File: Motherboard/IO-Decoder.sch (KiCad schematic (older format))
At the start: 7 parts, among them U28 8288, U29 74LS245, U30 74LS04, U31 74LS573, U32 74LS244, U33 74LS573

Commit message: Large sync
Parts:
- added RN2: R_Network04, Resistor_THT:R_Array_SIP5, symbol Device:R_Network04
- added U40: 74LS27, Housings_DIP:DIP-14_W7.62mm_Socket, symbol 74xx:74LS27
- added U41: 74LS04, Housings_DIP:DIP-14_W7.62mm_Socket, symbol 74xx:74LS04
- added U43, U44, U45: 74LS244, Housings_DIP:DIP-20_W7.62mm_Socket, symbol 74xx:74LS244
- added U46: 74LS245, Housings_DIP:DIP-20_W7.62mm_Socket, symbol 74xx:74LS245
- added U47: 4077, Housings_DIP:DIP-14_W7.62mm_Socket, symbol 4xxx:4077
- added U48: SST39SF010, Housings_DIP:DIP-32_W15.24mm_Socket, symbol Memory_Flash:SST39SF010
- added U49: 74LS243, Housings_DIP:DIP-12_W7.62mm_Socket, symbol 74xx:74LS243
- U29, U31, U32, U33: footprint (none) -> Housings_DIP:DIP-20_W7.62mm_Socket
- U30: footprint (none) -> Housings_DIP:DIP-14_W7.62mm_Socket
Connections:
- net labels added: AEN, CLK33, DACK0_BRD, DCLK, ROMADDR, XA0, XA1, XA10, XA11, XA12, XA13, XA14, XA15, XA16, XA17, XA18, XA19, XA2, XA3, XA4, XA5, XA6, XA7, XA8, XA9, XA[0...19], XCLK, XD0, XD1, XD2, XD3, XD4, XD5, XD6, XD7, XD[0...7], ~CS6, ~CS7, ~DACK0, ~DMAAEN, ~IOR, ~MEMR, ~XIOR, ~XIOW, ~XMEMR, ~XMEMW, ~YMEMW
- wire segments 91 -> 230
- no-connect marks 11 -> 13

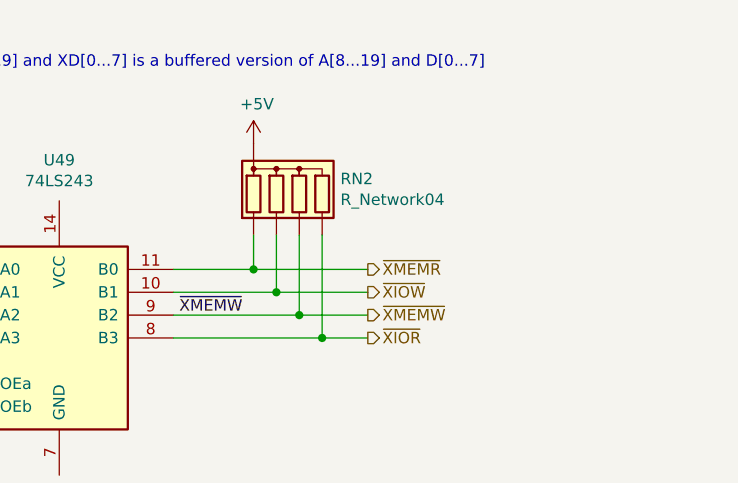
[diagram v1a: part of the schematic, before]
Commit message: Work on motherboard  - Integrating glue logic into CPLD  - Began work on routing
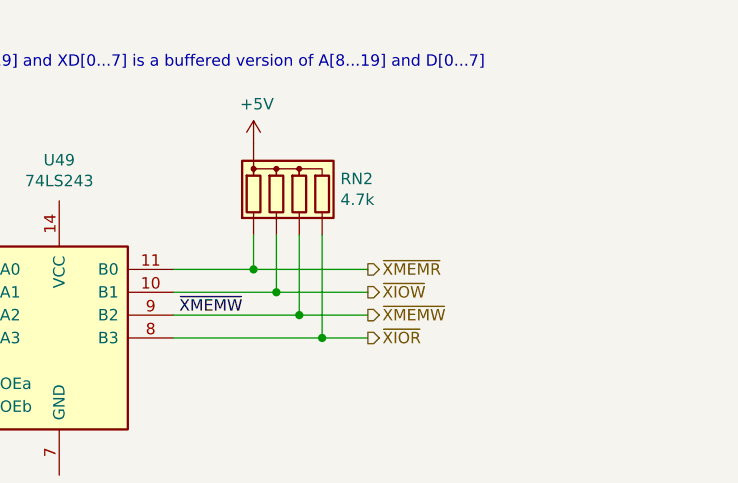
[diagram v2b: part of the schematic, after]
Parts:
- RN1: footprint Resistor_THT:R_Array_SIP6 -> Resistors_THT:R_Array_SIP6
- RN2: value R_Network04 -> 4.7k; footprint Resistor_THT:R_Array_SIP5 -> Resistors_THT:R_Array_SIP5
- U28: footprint Package_DIP:DIP-20_W7.62mm -> Housings_DIP:DIP-20_W7.62mm_Socket
- U49: footprint Housings_DIP:DIP-12_W7.62mm_Socket -> Housings_DIP:DIP-14_W7.62mm_Socket
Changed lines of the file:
@@
 F 0 "U28" H 2300 2800 50  0000 C CNN
 F 1 "8288" H 2300 2725 50  0000 C CNN
-F 2 "Package_DIP:DIP-20_W7.62mm" H 1925 1900 50  0001 C CIN
+F 2 "Housings_DIP:DIP-20_W7.62mm_Socket" H 1925 1900 50  0001 C CIN
 F 3 "http://www.datasheets360.com/pdf/7208679415653955300" H 1375 2700 50  0001 C CNN
 	1    1925 1900
@@
 F 0 "RN1" H 3280 1021 50  0000 L CNN
 F 1 "4.7k" H 3280 930 50  0000 L CNN
-F 2 "Resistor_THT:R_Array_SIP6" V 3375 975 50  0001 C CNN
+F 2 "Resistors_THT:R_Array_SIP6" V 3375 975 50  0001 C CNN
 F 3 "http://www.vishay.com/docs/31509/csc.pdf" H 3000 975 50  0001 C CNN
 	1    3000 975
@@
 F 0 "U49" H 13775 2728 50  0000 C CNN
 F 1 "74LS243" H 13775 2637 50  0000 C CNN
-F 2 "Housings_DIP:DIP-12_W7.62mm_Socket" H 13775 1950 50  0001 C CNN
+F 2 "Housings_DIP:DIP-14_W7.62mm_Socket" H 13775 1950 50  0001 C CNN
 F 3 "http://www.ti.com/lit/gpn/sn74LS243" H 13775 1950 50  0001 C CNN
 	1    13775 1950
@@
 P 14825 1300
 F 0 "RN2" H 15005 1346 50  0000 L CNN
-F 1 "R_Network04" H 15005 1255 50  0000 L CNN
-F 2 "Resistor_THT:R_Array_SIP5" V 15100 1300 50  0001 C CNN
+F 1 "4.7k" H 15005 1255 50  0000 L CNN
+F 2 "Resistors_THT:R_Array_SIP5" V 15100 1300 50  0001 C CNN
 F 3 "http://www.vishay.com/docs/31509/csc.pdf" H 14825 1300 50  0001 C CNN
 	1    14825 1300
@@
 Wire Bus Line
 	2225 9525 2625 9525
-Wire Bus Line
-	725  3700 725  6850
-Wire Bus Line
-	11175 4050 11175 5750
-Wire Bus Line
-	14675 4200 14675 5075
-Wire Bus Line
-	11200 7000 11200 8000
-Wire Bus Line
-	9650 7000 9650 7800
-Wire Bus Line
-	2825 4525 2825 5350
-Wire Bus Line
-	825  4300 825  5125
-Wire Bus Line
-	11175 1150 11175 4050
-Wire Bus Line
-	12825 4050 12825 5600
-Wire Bus Line
-	9650 1150 9650 5550
-Wire Bus Line
-	6400 1350 6400 6950
-Wire Bus Line
-	4175 1175 4175 6850
 Text Label 2625 9525 2    50   ~ 0
 XA[0...19]
 Text Label 2625 9625 2    50   ~ 0
 A[0...19]
+Wire Bus Line
+	725  3700 725  6850
+Wire Bus Line
+	11175 4050 11175 5750
+Wire Bus Line
+	14675 4200 14675 5075
+Wire Bus Line
+	11200 7000 11200 8000
+Wire Bus Line
+	9650 7000 9650 7800
+Wire Bus Line
+	2825 4525 2825 5350
+Wire Bus Line
+	825  4300 825  5125
+Wire Bus Line
+	11175 1150 11175 4050
+Wire Bus Line
+	12825 4050 12825 5600
+Wire Bus Line
+	9650 1150 9650 5550
+Wire Bus Line
+	6400 1350 6400 6950
+Wire Bus Line
+	4175 1175 4175 6850
 $EndSCHEMATC

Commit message: Some missed changes
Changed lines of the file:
@@
 Wire Wire Line
 	1350 5425 1475 5425
-Entry Bus Bus
-	725  4200 825  4300
 Entry Wire Line
 	825  4325 925  4425
@@
 A[0...19]
 Wire Bus Line
-	725  3700 725  6850
+	725  3700 725  4300
+Text Label 725  4125 1    50   ~ 0
+AD[0...19]
+Wire Bus Line
+	825  4300 725  4300
 Wire Bus Line
 	11175 4050 11175 5750
@@
 Wire Bus Line
 	4175 1175 4175 6850
+Connection ~ 725  4300
+Wire Bus Line
+	725  4300 725  6850
 $EndSCHEMATC

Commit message: Large sync
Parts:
- removed U47: 4077, Housings_DIP:DIP-14_W7.62mm_Socket, symbol 4xxx:4077
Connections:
- net labels added: N.P.NPI
- wire segments 230 -> 229
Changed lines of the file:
@@
 $Descr A3 16535 11693
 encoding utf-8
-Sheet 7 8
+Sheet 7 10
 Title ""
 Date ""
@@
 Wire Wire Line
 	12700 6300 13150 6300
-Wire Wire Line
-	12100 6200 11925 6200
-Wire Wire Line
-	12100 6400 11925 6400
-Text Label 11925 6200 0    50   ~ 0
-~CS7
-Text Label 11925 6400 0    50   ~ 0
-~CS6
 Text Label 12950 5600 0    50   ~ 0
 ~CS6
@@
 $EndComp
 $Comp
-L 4xxx:4077 U47
-U 1 1 5C9967BE
-P 12400 6300
-F 0 "U47" H 12400 6625 50  0000 C CNN
-F 1 "4077" H 12400 6534 50  0000 C CNN
-F 2 "Housings_DIP:DIP-14_W7.62mm_Socket" H 12400 6300 50  0001 C CNN
-F 3 "http://www.intersil.com/content/dam/Intersil/documents/cd40/cd4076bms.pdf" H 12400 6300 50  0001 C CNN
-	1    12400 6300
-	1    0    0    -1
-$EndComp
-$Comp
 L power:GND #PWR061
 U 1 1 5C996D4B
@@
 Wire Bus Line
 	825  4300 725  4300
+Connection ~ 725  4300
+Wire Bus Line
+	725  4300 725  6850
+Text HLabel 1300 10225 0    50   Output ~ 0
+N.P.NPI
+Wire Wire Line
+	1300 10225 1500 10225
 Wire Bus Line
 	11175 4050 11175 5750
@@
 Wire Bus Line
 	4175 1175 4175 6850
-Connection ~ 725  4300
-Wire Bus Line
-	725  4300 725  6850
+Text Label 12700 6300 0    50   ~ 0
+ROMADDR
 $EndSCHEMATC

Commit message: LARGE sync
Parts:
- added U42: AS6C8008, Package_SO:TSSOP-44_4.4x11.2mm_P0.5mm, symbol RAM:AS6C8008
- added U47: 74LS245, Package_DIP:DIP-20_W7.62mm_Socket, symbol 74xx:74LS245
- added U50: 7400, Package_DIP:DIP-14_W7.62mm_Socket, symbol 74xx:7400
- added U52: 74LS32, Package_DIP:DIP-14_W7.62mm_Socket, symbol 74xx:74LS32
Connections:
- net +5V: now also U43.20 (VCC), U49.14 (VCC), U42.11 (VCC), U42.33 (VCC), U42.40 (CE2), U47.20 (VCC)
- net GND: now also U43.10 (GND), U49.7 (GND), U42.12 (VSS), U42.34 (VSS), U47.10 (GND)
- net XA0: now also U42.5 (A0)
- net XA1: now also U42.4 (A1)
- net XA10: now also U42.27 (A10)
- net XA11: now also U42.26 (A11)
- net XA12: now also U42.25 (A12)
- net XA13: now also U42.24 (A13)
- net XA14: now also U42.23 (A14)
- net XA15: now also U42.22 (A15)
- net XA16: now also U42.21 (A16)
- net XA17: now also U42.20 (A17), U52.1
- net XA18: now also U42.19 (A18), U52.2
- net XA19: now also U42.18 (A19), U50.2
- net XA2: now also U42.3 (A2)
- net XA3: now also U42.2 (A3)
- net XA4: now also U42.1 (A4)
- net XA5: now also U42.44 (A5)
- net XA6: now also U42.43 (A6)
- net XA7: now also U42.42 (A7)
- net XA8: now also U42.39 (A8)
- net XA9: now also U42.28 (A9)
- net XD0: now also U47.2 (A0)
- net XD1: now also U47.3 (A1)
- net XD2: now also U47.4 (A2)
- net XD3: now also U47.5 (A3)
- net XD4: now also U47.6 (A4)
- net XD5: now also U47.7 (A5)
- net XD6: now also U47.8 (A6)
- net XD7: now also U47.9 (A7)
- net ~XMEMR: now also U42.41 (~OE), U47.1 (A->B)
- net ~XMEMW: now also U42.17 (~WE)
- new net: U42.10 (DQ1), U47.12 (B6)
- new net: U42.13 (DQ2), U47.13 (B5)
- new net: U42.14 (DQ3), U47.14 (B4)
- new net: U42.31 (DQ4), U47.15 (B3)
- new net: U42.32 (DQ5), U47.16 (B2)
- new net: U42.35 (DQ6), U47.17 (B1)
- new net: U42.36 (DQ7), U47.18 (B0)
- new net: U42.9 (DQ0), U47.11 (B7)
- new net: U50.1, U52.3
- new net ~RAMSEL: U42.6 (~CE), U47.19 (CE), U50.3
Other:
- note added: "BIOS ROM"
- note added: "RAM"
- note added: "XA[8...19] and XD[0...7] is a DMA version of A[8...19] and D[0...7]"
- note removed: "XA[8...19] and XD[0...7] is a buffered version of A[8...19] and D[0...7]"
- moved on the sheet: U40A, U40B, U41A

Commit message: end of day commit, routed major parts of the motherboard
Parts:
- U42: symbol RAM:AS6C8008 -> Motherboard-rescue:AS6C8008-RAM
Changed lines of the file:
@@
 EESchema Schematic File Version 4
 LIBS:Motherboard-cache
-EELAYER 29 0
+EELAYER 26 0
 EELAYER END
 $Descr A3 16535 11693
@@
 $EndComp
 $Comp
-L RAM:AS6C8008 U42
+L Motherboard-rescue:AS6C8008-RAM U42
 U 1 1 5CA57105
 P 5155 9710
+AR Path="/5CA57105" Ref="U42"  Part="1"
+AR Path="/5C32B2C3/5CA57105" Ref="U42"  Part="1"
 F 0 "U42" H 5155 11038 50  0000 C CNN
 F 1 "AS6C8008" H 5155 10947 50  0000 C CNN
